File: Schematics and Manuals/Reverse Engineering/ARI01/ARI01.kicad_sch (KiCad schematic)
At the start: 58 parts, among them J1 Conn_01x40, Q1 PNP, Q19 PNP, Q2 PNP, Q3 PNP, Q4 PNP, Q5 PNP, Q6 PNP

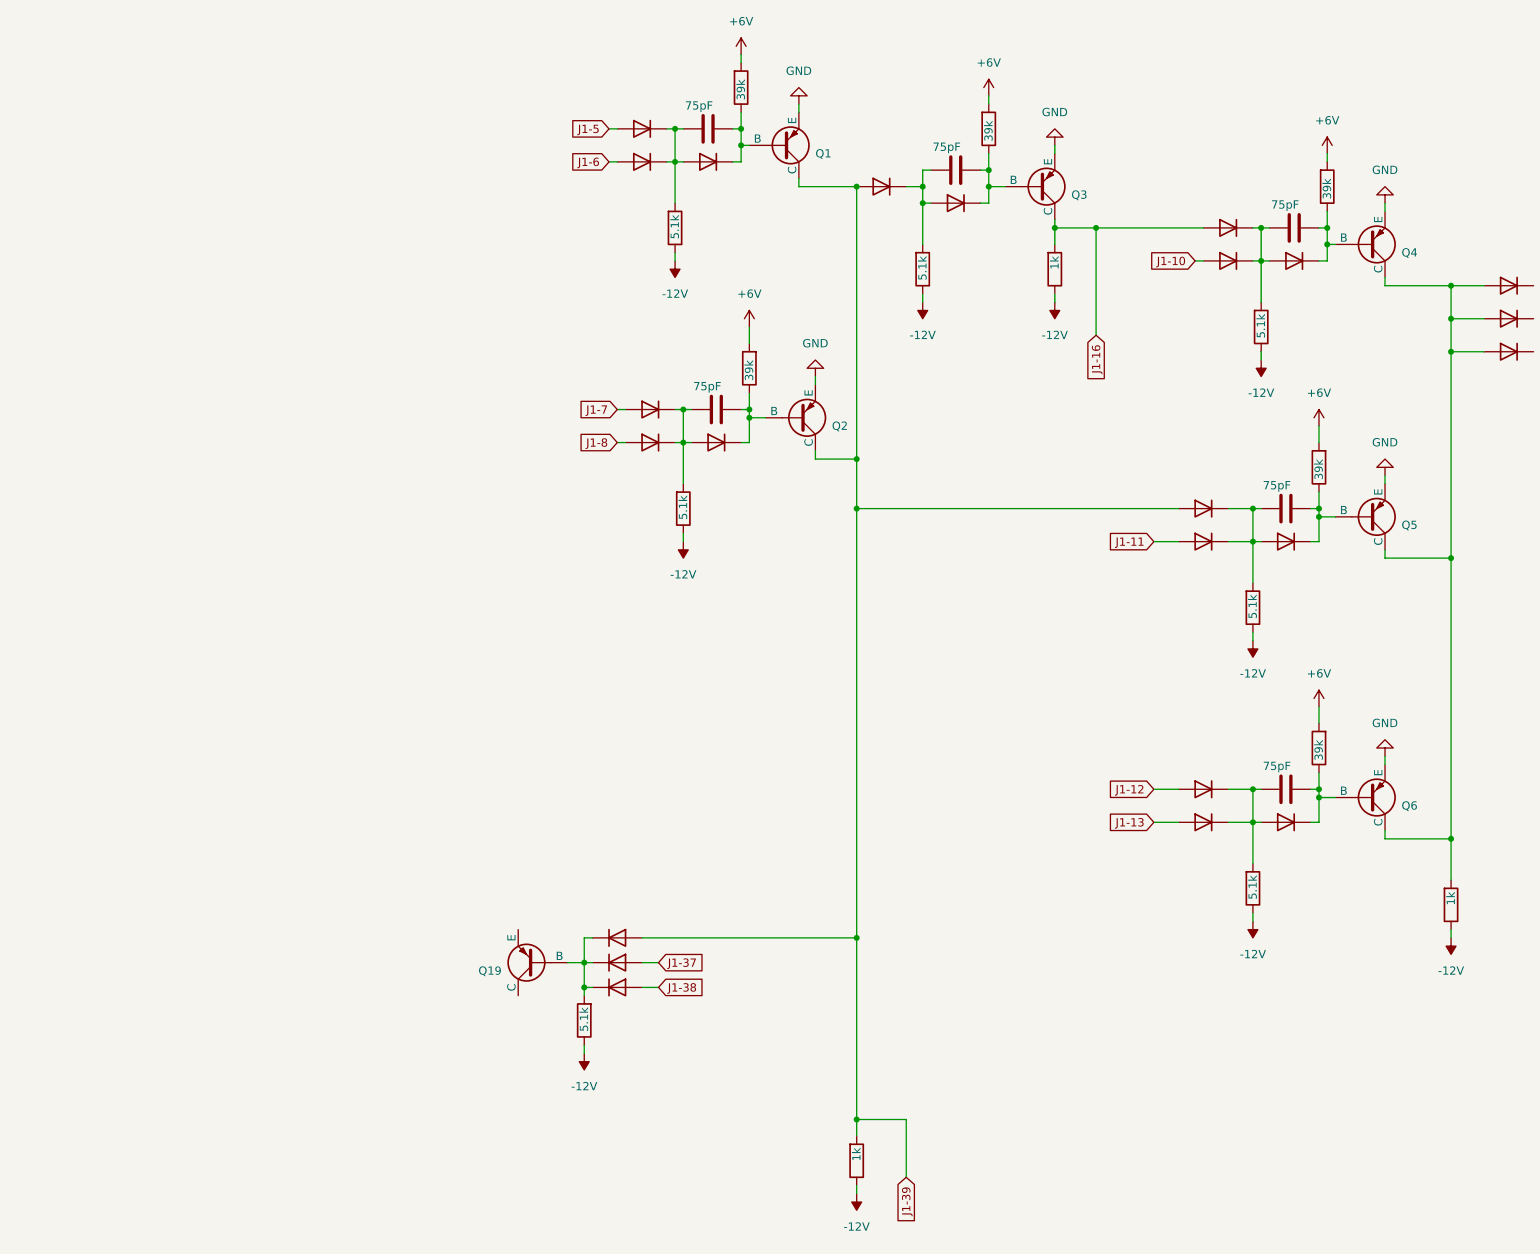
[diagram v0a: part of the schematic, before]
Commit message: Collector side of ARI01 Q19, and corrected some zener diodes
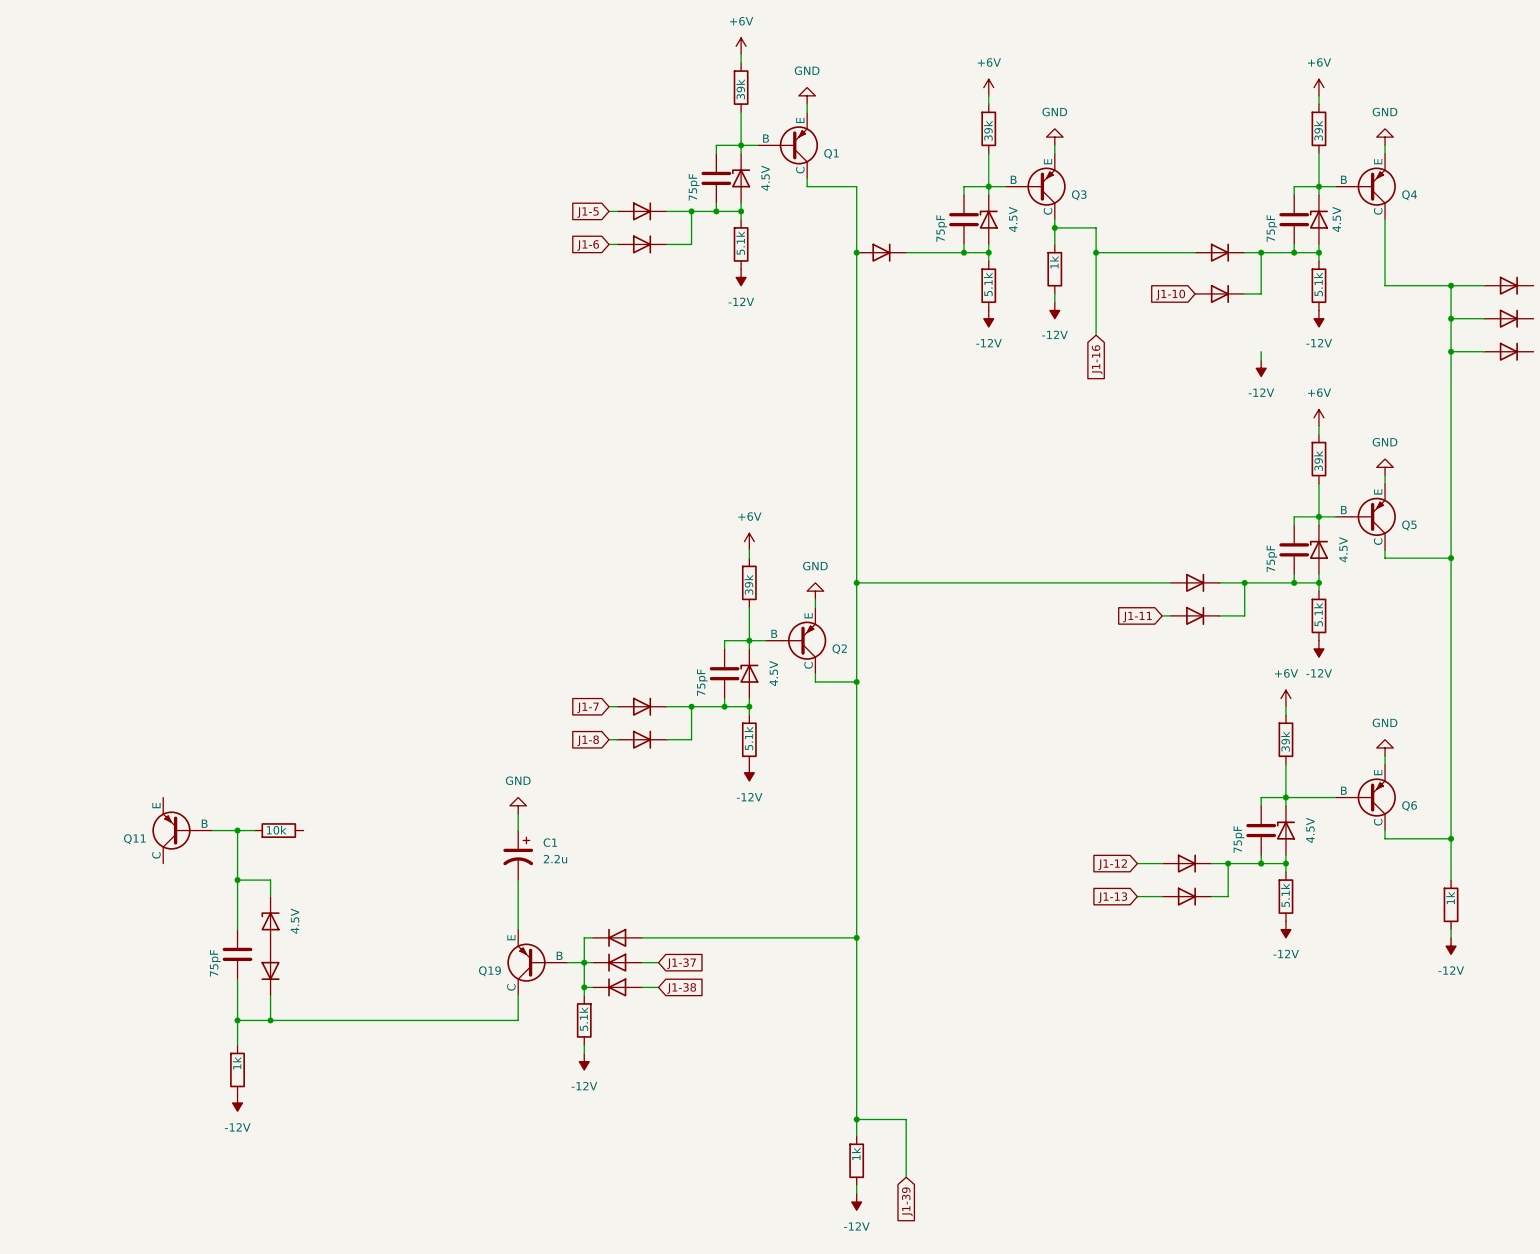
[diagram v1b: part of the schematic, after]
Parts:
- removed D35, D39, D42, D43, D55, D60: D, symbol Device:D
- removed R17, R19, R21: 5.1k, symbol Device:R
- removed R22: 39k, symbol Device:R
- added C1: 2.2u, symbol Device:C_Polarized_US
- added C2: 75pF, symbol Device:C
- added D1: S1005, symbol Device:D
- added D2, D3, D4, D5, D6, D7, D8: 4.5V, symbol Device:D_Zener
- added Q11: PNP, symbol Simulation_SPICE:PNP
- added R1, R3, R5: 39k, symbol Device:R
- added R2, R4, R6: 5.1k, symbol Device:R
- R10, R11: value 39k -> 5.1k
- R12: value 5.1k -> 1k
- R14: value 5.1k -> 10k
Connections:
- net +6V: now also R1.2, R3.2, R5.2; no longer R10.2, R11.2
- net -12V: now also R10.1, R11.1, R2.1, R4.1, R6.1; no longer R14.1
- net GND: now also C1.1
- net at C4.2, D52.1 (K), D53.1 (K): now also R10.2, D6.2 (A); no longer R14.2
- net at C4.1, Q2.2 (B), R8.1: now also D6.1 (K)
- net at D61.1 (K), D62.1 (K): now also C7.2, D5.2 (A), R6.2; no longer C8.2
- net at Q6.2 (B): now also C7.1, D5.1 (K), R5.1; no longer C8.1
- net at C6.1, Q5.2 (B): now also D4.1 (K), R3.1; no longer R10.1
- net at C6.2, D44.1 (K), D45.1 (K): now also D4.2 (A), R4.2
- net at C3.2, D38.1 (K), D51.1 (K): now also R11.2, D7.2 (A); no longer R12.2
- net at C5.1, Q3.2 (B), R9.1: now also D2.1 (K)
- net at D54.1 (K), D56.1 (K): now also C2.2, D3.2 (A), R2.2; no longer C7.2
- net at C3.1, Q1.2 (B), R7.1: now also D7.1 (K)
- net at C5.2, D36.1 (K), R16.2: now also D2.2 (A)
- net at Q19.1 (C): now also C8.2, R12.2, D1.1 (K)
- net at Q19.3 (E): now also C1.2
- new net: C8.1, D8.1 (K), Q11.2 (B), R14.2
- new net: D1.2 (A), D8.2 (A)
- new net: C2.1, D3.1 (K), Q4.2 (B), R1.1
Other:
- moved on the sheet: Q1, Q2, Q4

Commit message: Most of Q15-19 reverse engineering done
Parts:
- added C9: 75pF, symbol Device:C
- added D10, D11, D12, D13, D14, D15, D16, D17, D9: D, symbol Device:D
- added D18: 4.5V, symbol Device:D_Zener
- added D19: S1005, symbol Device:D
- added Q12, Q15, Q16, Q17, Q18: PNP, symbol Simulation_SPICE:PNP
- added R17: 51k, symbol Device:R
- added R19, R21, R22: 5.1k, symbol Device:R
- added R23: 1k, symbol Device:R
- added R24: 10k, symbol Device:R
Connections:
- net J1-26 is gone; now on net GND: J1.26 (Pin_26)
- net -12V: now also R17.1, R19.1, R21.1, R22.1, R23.1
- net GND: now also Q12.3 (E)
- net J1-28: now also D15.2 (A)
- net J1-29: now also D16.2 (A)
- net J1-30: now also D17.2 (A), Q12.1 (C), R23.2
- net J1-31: now also D13.2 (A)
- net J1-32: now also D14.2 (A)
- net J1-33: now also D11.2 (A)
- net J1-34: now also D12.2 (A)
- net J1-35: now also D9.2 (A)
- net J1-36: now also D10.2 (A)
- net at C8.2, D1.1 (K), Q19.1 (C)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: now also Q15.1 (C), Q16.1 (C), Q17.1 (C), Q18.1 (C)
- net at C8.1, D8.1 (K), Q11.2 (B): now also R14.1; no longer R14.2
- net at C1.2, Q19.3 (E): now also Q15.3 (E), Q16.3 (E), Q17.3 (E), Q18.3 (E)
- new net: D13.1 (K), D14.1 (K), Q16.2 (B), R21.2
- new net: C9.1, D18.1 (K), Q12.2 (B), R24.1
- new net: D15.1 (K), D16.1 (K), D17.1 (K), Q15.2 (B), R22.2
- new net: D11.1 (K), D12.1 (K), Q17.2 (B), R19.2
- new net: C9.2, D19.1 (K)
- new net: D10.1 (K), D9.1 (K), Q18.2 (B), R17.2
- new net: D18.2 (A), D19.2 (A)
- no-connect marks 0 -> 1
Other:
- moved on the sheet: Q11

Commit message: Traced Q21-24 area and -1V rail
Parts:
- added C10: 2.2u, symbol Device:C_Polarized_US
- added D20, D21, D22: S1005, symbol Device:D
- added D23, D24, D25, D26, D27, D28, D29, D30, D31, D32, D33, D34: D, symbol Device:D
- added Q20, Q21, Q22, Q23, Q24, Q7: PNP, symbol Simulation_SPICE:PNP
- added R25, R27, R28, R29, R30: 5.1k, symbol Device:R
- added R26, R31: 1k, symbol Device:R
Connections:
- net +6V: now also R14.2, R24.2, C10.1
- net -12V: now also R25.1, R26.1, R27.1, R28.1, R29.1, R30.1, R31.1; no longer R23.1
- net GND: now also C10.2, D21.2 (A), Q20.3 (E), Q7.3 (E)
- net J1-17: now also D30.2 (A), D33.2 (A)
- net J1-18: now also D25.2 (A), D28.2 (A)
- net J1-38: now also D27.2 (A), D34.2 (A)
- net at D57.2 (A), D58.2 (A), D59.2 (A)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: now also D24.2 (A), D32.2 (A)
- net -1V: now reaches C1.2, Q15.3 (E), Q16.3 (E), Q17.3 (E), Q18.3 (E), Q19.3 (E)
- net -1V: now also D22.1 (K), Q21.3 (E), Q22.3 (E), Q23.3 (E), Q24.3 (E), R25.2
- net at C9.2, D19.1 (K): now also Q21.1 (C), Q22.1 (C), Q23.1 (C), Q24.1 (C), R26.2
- new net: D23.1 (K), D24.1 (K), D25.1 (K), Q24.2 (B), R27.2
- new net: D32.1 (K), D33.1 (K), D34.1 (K), Q21.2 (B), R30.2
- new net: D20.1 (K), D22.2 (A)
- new net: D23.2 (A), D31.2 (A), Q20.1 (C), R31.2
- new net: D26.1 (K), D27.1 (K), D28.1 (K), Q23.2 (B), R28.2
- new net: D26.2 (A), D29.2 (A), Q7.1 (C)
- new net: D29.1 (K), D30.1 (K), D31.1 (K), Q22.2 (B), R29.2
- new net: D20.2 (A), D21.1 (K)
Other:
- moved on the sheet: C1, Q11, Q12

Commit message: Circuit RE complete, probably
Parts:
- removed D47, D48, D50, D58: D, symbol Device:D
- added C11, C12, C13, C14, C15, C16, C17: 75pF, symbol Device:C
- added D35, D39, D43, D55, D60: S1005, symbol Device:D
- added D42: ???, symbol Device:D_Zener
- added D47, D48, D50, D58, D63, D66: 4.5V, symbol Device:D_Zener
- added D64, D65, D67, D68: D, symbol Device:D
- added Q10, Q13, Q14, Q8, Q9: PNP, symbol Simulation_SPICE:PNP
- added R32, R37, R49: 1k, symbol Device:R
- added R33, R36, R39, R44, R45, R47: 5.1k, symbol Device:R
- added R34, R35, R38, R42, R43, R46, R48: 39k, symbol Device:R
- added R40, R41: 680, symbol Device:R
- D57: value D -> S1005
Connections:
- net J1-24 is gone; now on net GND: J1.24 (Pin_24)
- net +6V: now also R34.2, R35.2, R38.2, R42.2, R43.2, R46.2, R48.2
- net -12V: now also D35.2 (A), D43.2 (A), R32.1, R33.1, R36.1, R37.1, R39.1, R41.1, R44.1, R45.1, R47.1, R49.1
- net GND: now also Q11.3 (E), Q10.3 (E), Q13.3 (E), Q14.3 (E), Q8.3 (E), Q9.3 (E), R40.2
- net J1-18: now also D65.2 (A)
- net J1-19: now also Q8.1 (C), R37.2
- net J1-20: now also D49.2 (A), Q13.1 (C), Q14.1 (C), Q9.1 (C), R40.1, R41.2
- net J1-21: now also D60.2 (A)
- net J1-23: now also D43.1 (K), Q10.1 (C)
- net J1-25: now also Q11.1 (C), D35.1 (K), D39.2 (A), R32.2
- net J1-38: now also D57.2 (A), D64.2 (A), D67.2 (A); no longer D49.2 (A)
- net at D24.2 (A), D32.2 (A), D59.2 (A)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: no longer D57.2 (A)
- net at D26.2 (A), D29.2 (A), Q7.1 (C): now also D55.2 (A), D68.2 (A), R49.2
- net at D49.1 (K): now also C13.2, D48.2 (A), R39.2
- net at D59.1 (K): now also C15.2, D58.2 (A), R44.2
- net at Q20.2 (B): now also C12.1, D47.1 (K), R35.1
- net at D57.1 (K): now also C14.2, D50.2 (A), D55.1 (K), D60.1 (K), R45.2
- net at Q7.2 (B): now also C15.1, D58.1 (K), R43.1
- net at D46.1 (K): now also C12.2, D47.2 (A), R36.2
- new net: C16.2, D63.2 (A), D64.1 (K), D65.1 (K), R47.2
- new net: C14.1, D50.1 (K), Q9.2 (B), R42.1
- new net: C16.1, D63.1 (K), Q13.2 (B), R46.1
- new net: C17.2, D66.2 (A), D67.1 (K), D68.1 (K)
- new net: C13.1, D48.1 (K), Q8.2 (B), R38.1
- new net: C11.2, D39.1 (K), D42.2 (A), R33.2
- new net: C11.1, D42.1 (K), Q10.2 (B), R34.1
- new net: C17.1, D66.1 (K), Q14.2 (B), R48.1
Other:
- moved on the sheet: J1, Q1, Q11, Q12, Q15, Q16, Q17, Q18, Q19, Q2, Q20, Q21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
